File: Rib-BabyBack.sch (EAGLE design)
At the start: 23 parts, among them IC1 REG1117, SW1 DPDT

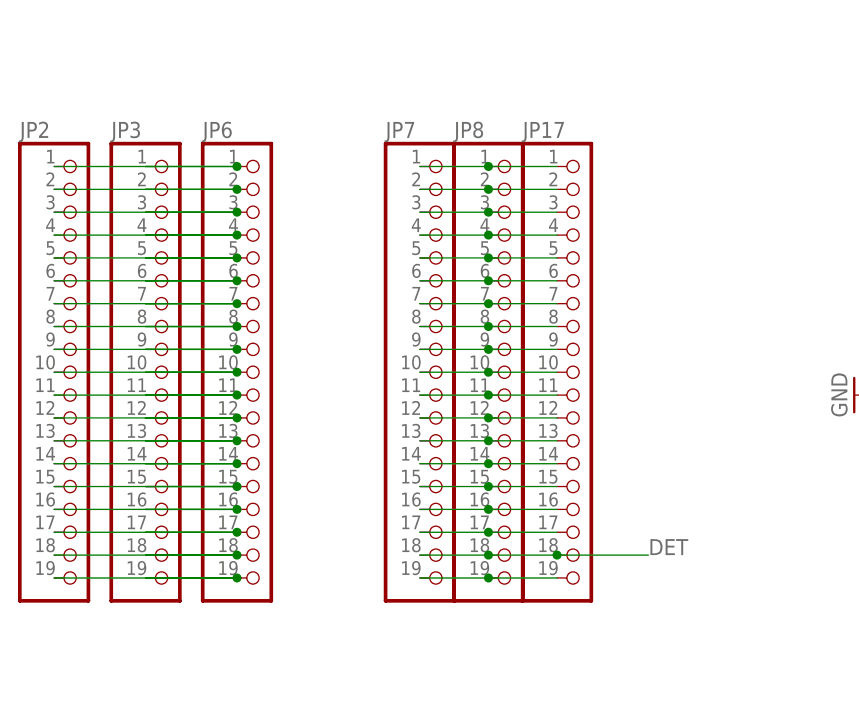
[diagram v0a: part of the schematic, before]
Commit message: Issue #26 Disconnect specific IO used by System Resources on ESP32
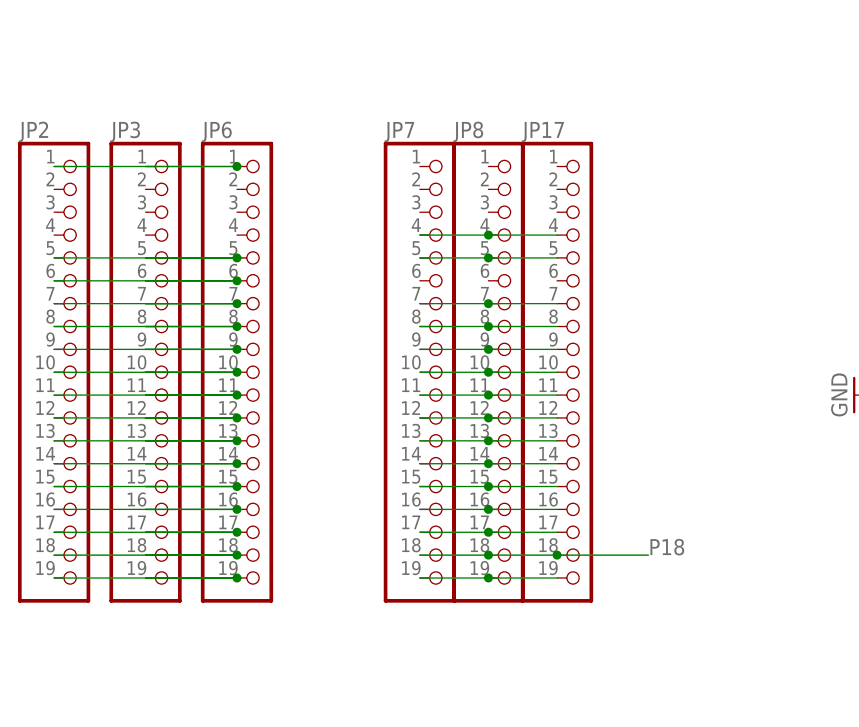
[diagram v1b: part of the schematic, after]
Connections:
- removed net N$14: JP2.9, JP3.9, JP6.9
- removed net N$25: JP17.1, JP7.1, JP8.1
- removed net N$26: JP17.2, JP7.2, JP8.2
- removed net N$27: JP17.3, JP7.3, JP8.3
- removed net N$30: JP17.6, JP7.6, JP8.6
- removed net N$7: JP2.2, JP3.2, JP6.2
- removed net N$8: JP2.3, JP3.3, JP6.3
- removed net N$9: JP2.4, JP3.4, JP6.4
- new net P18: JP17.18, JP7.18, JP8.18
- net DET: now also JP2.9, JP3.9, JP6.9; no longer JP17.18, JP7.18, JP8.18
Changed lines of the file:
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@@
-</segment>
-</net>
-<net name="N$7" class="0">
-<segment>
-<pinref part="JP2" gate="G$1" pin="2"/>
-<pinref part="JP3" gate="G$1" pin="2"/>
-<wire x1="-78.74" y1="-152.4" x2="-58.42" y2="-152.4" width="0.1524" layer="91"/>
-<pinref part="JP6" gate="G$1" pin="2"/>
-<junction x="-58.42" y="-152.4"/>
-<wire x1="-58.42" y1="-152.4" x2="-68.58" y2="-152.4" width="0.1524" layer="91"/>
-</segment>
-</net>
-<net name="N$8" class="0">
-<segment>
-<pinref part="JP2" gate="G$1" pin="3"/>
-<pinref part="JP3" gate="G$1" pin="3"/>
-<wire x1="-78.74" y1="-154.94" x2="-58.42" y2="-154.94" width="0.1524" layer="91"/>
-<pinref part="JP6" gate="G$1" pin="3"/>
-<junction x="-58.42" y="-154.94"/>
-<wire x1="-58.42" y1="-154.94" x2="-68.58" y2="-154.94" width="0.1524" layer="91"/>
-</segment>
-</net>
-<net name="N$9" class="0">
-<segment>
-<pinref part="JP2" gate="G$1" pin="4"/>
-<pinref part="JP3" gate="G$1" pin="4"/>
-<wire x1="-78.74" y1="-157.48" x2="-58.42" y2="-157.48" width="0.1524" layer="91"/>
-<pinref part="JP6" gate="G$1" pin="4"/>
-<junction x="-58.42" y="-157.48"/>
-<wire x1="-58.42" y1="-157.48" x2="-68.58" y2="-157.48" width="0.1524" layer="91"/>
 </segment>
 </net>
@@
 </segment>
 </net>
-<net name="N$14" class="0">
-<segment>
-<pinref part="JP2" gate="G$1" pin="9"/>
-<pinref part="JP3" gate="G$1" pin="9"/>
-<wire x1="-78.74" y1="-170.18" x2="-58.42" y2="-170.18" width="0.1524" layer="91"/>
-<pinref part="JP6" gate="G$1" pin="9"/>
-<junction x="-58.42" y="-170.18"/>
-<wire x1="-58.42" y1="-170.18" x2="-68.58" y2="-170.18" width="0.1524" layer="91"/>
-</segment>
-</net>
 <net name="N$15" class="0">
 <segment>
@@
 </segment>
 </net>
-<net name="N$25" class="0">
-<segment>
-<pinref part="JP8" gate="G$1" pin="1"/>
-<pinref part="JP17" gate="G$1" pin="1"/>
-<wire x1="-22.86" y1="-149.86" x2="-30.48" y2="-149.86" width="0.1524" layer="91"/>
-<pinref part="JP7" gate="G$1" pin="1"/>
-<junction x="-30.48" y="-149.86"/>
-<wire x1="-30.48" y1="-149.86" x2="-38.1" y2="-149.86" width="0.1524" layer="91"/>
-</segment>
-</net>
-<net name="N$26" class="0">
-<segment>
-<pinref part="JP8" gate="G$1" pin="2"/>
-<pinref part="JP17" gate="G$1" pin="2"/>
-<wire x1="-22.86" y1="-152.4" x2="-30.48" y2="-152.4" width="0.1524" layer="91"/>
-<pinref part="JP7" gate="G$1" pin="2"/>
-<junction x="-30.48" y="-152.4"/>
-<wire x1="-30.48" y1="-152.4" x2="-38.1" y2="-152.4" width="0.1524" layer="91"/>
-</segment>
-</net>
-<net name="N$27" class="0">
-<segment>
-<pinref part="JP8" gate="G$1" pin="3"/>
-<pinref part="JP17" gate="G$1" pin="3"/>
-<wire x1="-22.86" y1="-154.94" x2="-30.48" y2="-154.94" width="0.1524" layer="91"/>
-<pinref part="JP7" gate="G$1" pin="3"/>
-<junction x="-30.48" y="-154.94"/>
-<wire x1="-30.48" y1="-154.94" x2="-38.1" y2="-154.94" width="0.1524" layer="91"/>
-</segment>
-</net>
 <net name="N$28" class="0">
 <segment>
@@
 <junction x="-30.48" y="-160.02"/>
 <wire x1="-30.48" y1="-160.02" x2="-38.1" y2="-160.02" width="0.1524" layer="91"/>
-</segment>
-</net>
-<net name="N$30" class="0">
-<segment>
-<pinref part="JP8" gate="G$1" pin="6"/>
-<pinref part="JP17" gate="G$1" pin="6"/>
-<wire x1="-22.86" y1="-162.56" x2="-30.48" y2="-162.56" width="0.1524" layer="91"/>
-<pinref part="JP7" gate="G$1" pin="6"/>
-<junction x="-30.48" y="-162.56"/>
-<wire x1="-30.48" y1="-162.56" x2="-38.1" y2="-162.56" width="0.1524" layer="91"/>
 </segment>
 </net>
@@
 <net name="DET" class="0">
 <segment>
+<pinref part="U$5" gate="G$1" pin="ATT"/>
+<wire x1="30.48" y1="-177.8" x2="20.32" y2="-177.8" width="0.1524" layer="91"/>
+</segment>
+<segment>
+<pinref part="JP2" gate="G$1" pin="9"/>
+<pinref part="JP3" gate="G$1" pin="9"/>
+<wire x1="-78.74" y1="-170.18" x2="-58.42" y2="-170.18" width="0.1524" layer="91"/>
+<pinref part="JP6" gate="G$1" pin="9"/>
+<junction x="-58.42" y="-170.18"/>
+<wire x1="-58.42" y1="-170.18" x2="-68.58" y2="-170.18" width="0.1524" layer="91"/>
+</segment>
+</net>
+<net name="N$24" class="0">
+<segment>
+<pinref part="R1" gate="G$1" pin="1"/>
+<pinref part="LED1" gate="G$1" pin="A"/>
+<wire x1="96.52" y1="-106.68" x2="96.52" y2="-109.22" width="0.1524" layer="91"/>
+</segment>
+</net>
+<net name="N$37" class="0">
+<segment>
+<pinref part="R2" gate="G$1" pin="1"/>
+<pinref part="LED2" gate="G$1" pin="A"/>
+<wire x1="111.76" y1="-106.68" x2="111.76" y2="-109.22" width="0.1524" layer="91"/>
+</segment>
+</net>
+<net name="N$38" class="0">
+<segment>
+<pinref part="R3" gate="G$1" pin="1"/>
+<pinref part="LED3" gate="G$1" pin="A"/>
+<wire x1="127" y1="-106.68" x2="127" y2="-109.22" width="0.1524" layer="91"/>
+</segment>
+</net>
+<net name="P18" class="0">
+<segment>
 <pinref part="JP17" gate="G$1" pin="18"/>
 <pinref part="JP8" gate="G$1" pin="18"/>
@@
 <label x="-12.7" y="-193.04" size="1.778" layer="95"/>
 </segment>
-<segment>
-<pinref part="U$5" gate="G$1" pin="ATT"/>
-<wire x1="30.48" y1="-177.8" x2="20.32" y2="-177.8" width="0.1524" layer="91"/>
-</segment>
-</net>
-<net name="N$24" class="0">
-<segment>
-<pinref part="R1" gate="G$1" pin="1"/>
-<pinref part="LED1" gate="G$1" pin="A"/>
-<wire x1="96.52" y1="-106.68" x2="96.52" y2="-109.22" width="0.1524" layer="91"/>
-</segment>
-</net>
-<net name="N$37" class="0">
-<segment>
-<pinref part="R2" gate="G$1" pin="1"/>
-<pinref part="LED2" gate="G$1" pin="A"/>
-<wire x1="111.76" y1="-106.68" x2="111.76" y2="-109.22" width="0.1524" layer="91"/>
-</segment>
-</net>
-<net name="N$38" class="0">
-<segment>
-<pinref part="R3" gate="G$1" pin="1"/>
-<pinref part="LED3" gate="G$1" pin="A"/>
-<wire x1="127" y1="-106.68" x2="127" y2="-109.22" width="0.1524" layer="91"/>
-</segment>
-</net>
+</net>

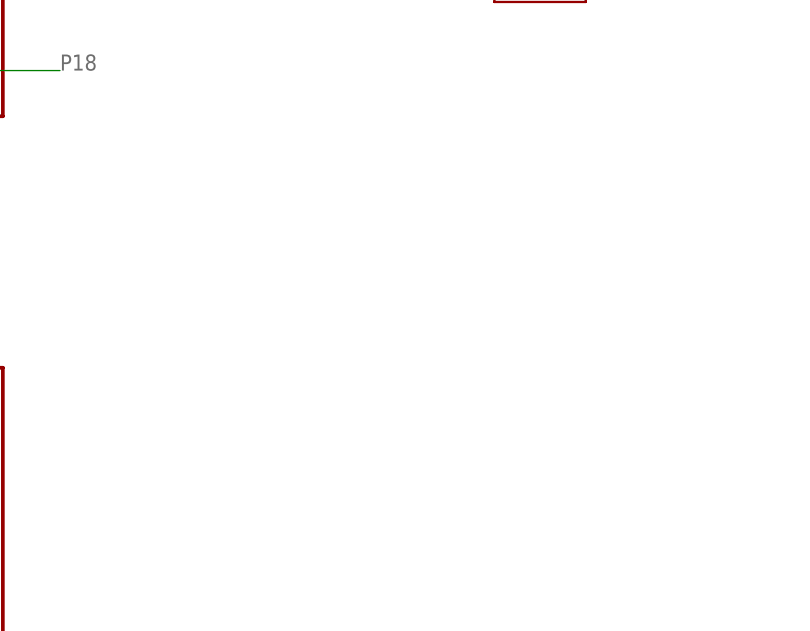
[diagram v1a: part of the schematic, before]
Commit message: Issue #32 ESP32 needs a user accessible LED on 13
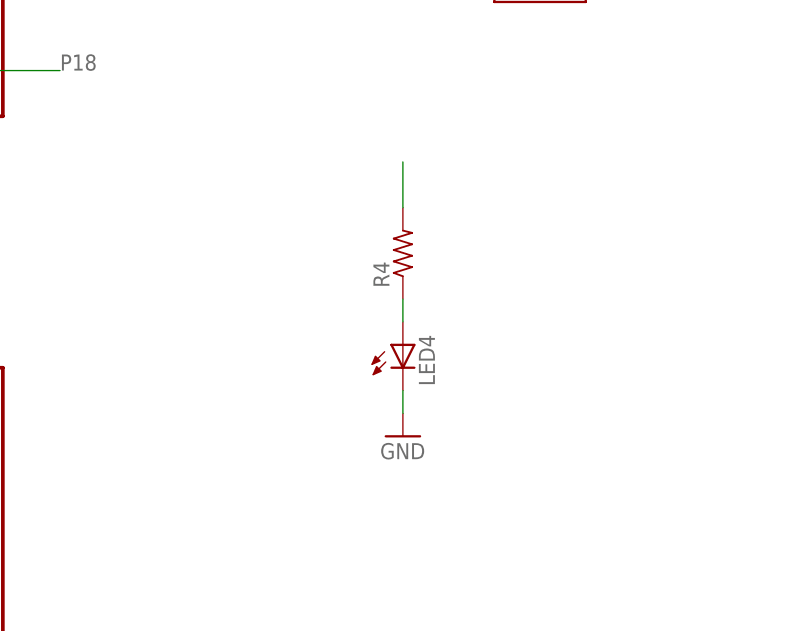
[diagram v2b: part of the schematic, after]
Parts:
- added LED4: (no value), eagle-ltspice:LED_ESML0603
- added R4: (no value), resistor:R-US_R0603
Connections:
- removed net N$10: JP2.5, JP3.5, JP6.5
- new net N$1: LED4.A, R4.1
- new net P13: JP2.5, JP3.5, JP6.5, R4.2
- net GND: now also LED4.C
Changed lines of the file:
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@@
 <part name="R2" library="resistor" library_urn="urn:adsk.eagle:library:348" deviceset="R-US_" device="R0603" package3d_urn="urn:adsk.eagle:package:26057/1"/>
 <part name="R3" library="resistor" library_urn="urn:adsk.eagle:library:348" deviceset="R-US_" device="R0603" package3d_urn="urn:adsk.eagle:package:26057/1"/>
+<part name="LED4" library="eagle-ltspice" library_urn="urn:adsk.eagle:library:217" deviceset="LED_E" device="SML0603" package3d_urn="urn:adsk.eagle:package:13315/1"/>
+<part name="GND6" library="supply1" library_urn="urn:adsk.eagle:library:371" deviceset="GND" device=""/>
+<part name="R4" library="resistor" library_urn="urn:adsk.eagle:library:348" deviceset="R-US_" device="R0603" package3d_urn="urn:adsk.eagle:package:26057/1"/>
 </parts>
 <sheets>
@@
 <instance part="R2" gate="G$1" x="111.76" y="-101.6" rot="R90"/>
 <instance part="R3" gate="G$1" x="127" y="-101.6" rot="R90"/>
+<instance part="LED4" gate="G$1" x="25.4" y="-223.52"/>
+<instance part="GND6" gate="1" x="25.4" y="-233.68"/>
+<instance part="R4" gate="G$1" x="25.4" y="-213.36" rot="R90"/>
 </instances>
 <busses>
@@
 <segment>
 <wire x1="55.88" y1="33.02" x2="50.8" y2="33.02" width="0.1524" layer="91"/>
-</segment>
-</net>
-<net name="N$10" class="0">
-<segment>
-<pinref part="JP2" gate="G$1" pin="5"/>
-<pinref part="JP3" gate="G$1" pin="5"/>
-<wire x1="-78.74" y1="-160.02" x2="-58.42" y2="-160.02" width="0.1524" layer="91"/>
-<pinref part="JP6" gate="G$1" pin="5"/>
-<junction x="-58.42" y="-160.02"/>
-<wire x1="-58.42" y1="-160.02" x2="-68.58" y2="-160.02" width="0.1524" layer="91"/>
 </segment>
 </net>
@@
 <wire x1="96.52" y1="-116.84" x2="96.52" y2="-119.38" width="0.1524" layer="91"/>
 </segment>
+<segment>
+<pinref part="LED4" gate="G$1" pin="C"/>
+<pinref part="GND6" gate="1" pin="GND"/>
+<wire x1="25.4" y1="-228.6" x2="25.4" y2="-231.14" width="0.1524" layer="91"/>
+</segment>
 </net>
 <net name="VCC" class="0">
@@
 </segment>
 </net>
+<net name="P13" class="0">
+<segment>
+<pinref part="R4" gate="G$1" pin="2"/>
+<wire x1="25.4" y1="-208.28" x2="25.4" y2="-203.2" width="0.1524" layer="91"/>
+</segment>
+<segment>
+<pinref part="JP2" gate="G$1" pin="5"/>
+<pinref part="JP3" gate="G$1" pin="5"/>
+<wire x1="-78.74" y1="-160.02" x2="-58.42" y2="-160.02" width="0.1524" layer="91"/>
+<pinref part="JP6" gate="G$1" pin="5"/>
+<junction x="-58.42" y="-160.02"/>
+<wire x1="-58.42" y1="-160.02" x2="-68.58" y2="-160.02" width="0.1524" layer="91"/>
+</segment>
+</net>
+<net name="N$1" class="0">
+<segment>
+<pinref part="R4" gate="G$1" pin="1"/>
+<pinref part="LED4" gate="G$1" pin="A"/>
+<wire x1="25.4" y1="-218.44" x2="25.4" y2="-220.98" width="0.1524" layer="91"/>
+</segment>
+</net>

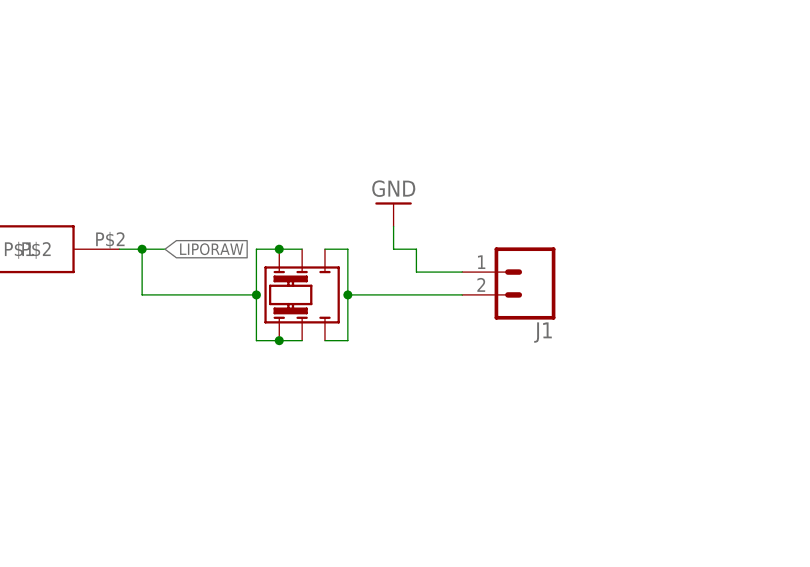
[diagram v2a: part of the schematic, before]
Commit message: Issue #22 Solder lugs resized to 3MM diameter holes and moved
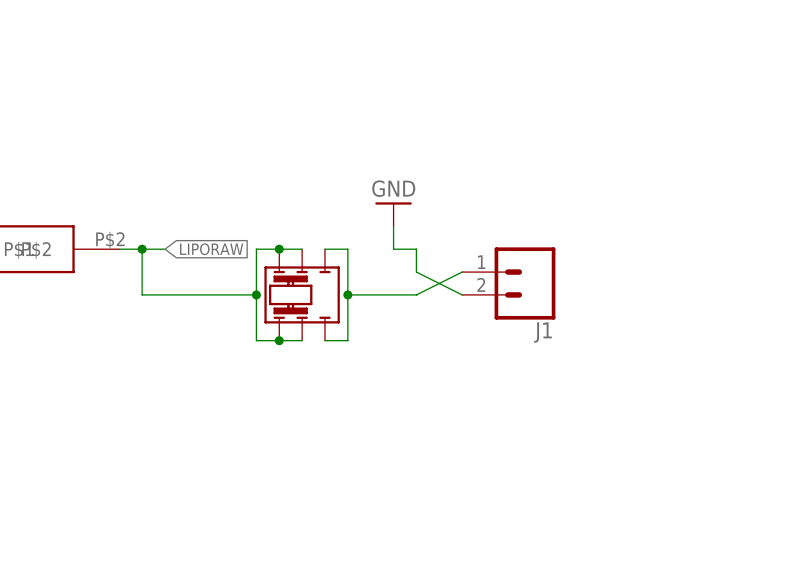
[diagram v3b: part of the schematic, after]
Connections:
- net GND: now also J1.2; no longer J1.1
- net N$11: now also J1.1; no longer J1.2
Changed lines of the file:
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@@
 <wire x1="71.12" y1="-53.34" x2="71.12" y2="-55.88" width="0.1524" layer="91"/>
 <wire x1="71.12" y1="-55.88" x2="73.66" y2="-55.88" width="0.1524" layer="91"/>
-<pinref part="J1" gate="G$1" pin="1"/>
-<wire x1="78.74" y1="-58.42" x2="73.66" y2="-58.42" width="0.1524" layer="91"/>
 <wire x1="73.66" y1="-58.42" x2="73.66" y2="-55.88" width="0.1524" layer="91"/>
+<pinref part="J1" gate="G$1" pin="2"/>
+<wire x1="78.74" y1="-60.96" x2="73.66" y2="-58.42" width="0.1524" layer="91"/>
 </segment>
 <segment>
@@
 <segment>
 <wire x1="66.04" y1="-66.04" x2="66.04" y2="-60.96" width="0.1524" layer="91"/>
+<pinref part="SW1" gate="G$1" pin="C2"/>
 <wire x1="66.04" y1="-60.96" x2="66.04" y2="-55.88" width="0.1524" layer="91"/>
-<wire x1="78.74" y1="-60.96" x2="66.04" y2="-60.96" width="0.1524" layer="91"/>
-<junction x="66.04" y="-60.96"/>
-<pinref part="SW1" gate="G$1" pin="C2"/>
 <wire x1="66.04" y1="-66.04" x2="63.5" y2="-66.04" width="0.1524" layer="91"/>
 <pinref part="SW1" gate="G$1" pin="C1"/>
 <wire x1="66.04" y1="-55.88" x2="63.5" y2="-55.88" width="0.1524" layer="91"/>
-<pinref part="J1" gate="G$1" pin="2"/>
-</segment>
-</net>
+<wire x1="66.04" y1="-60.96" x2="73.66" y2="-60.96" width="0.1524" layer="91"/>
+<junction x="66.04" y="-60.96"/>
+<pinref part="J1" gate="G$1" pin="1"/>
+<wire x1="73.66" y1="-60.96" x2="78.74" y2="-58.42" width="0.1524" layer="91"/>
+</segment>
+</net>

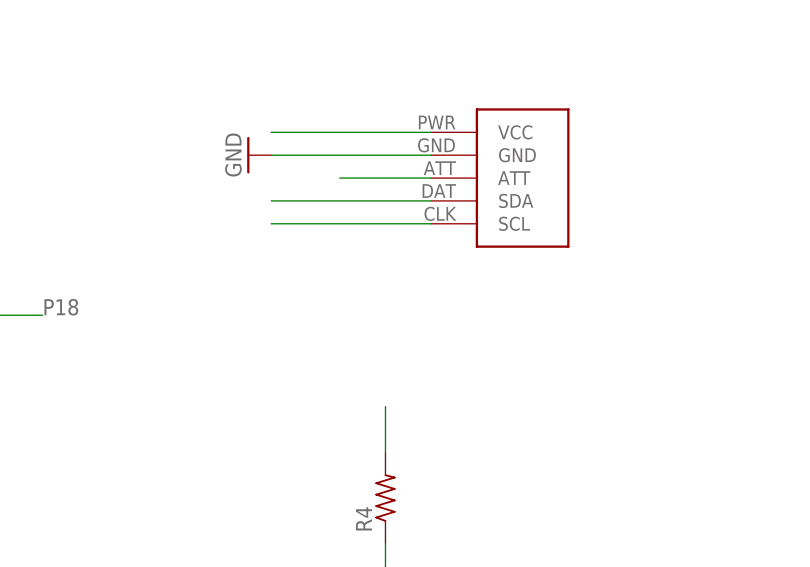
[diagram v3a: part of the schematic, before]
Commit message: Issue #19 4k7 ohm pullups to 3.3v are needed on SDA and SCL
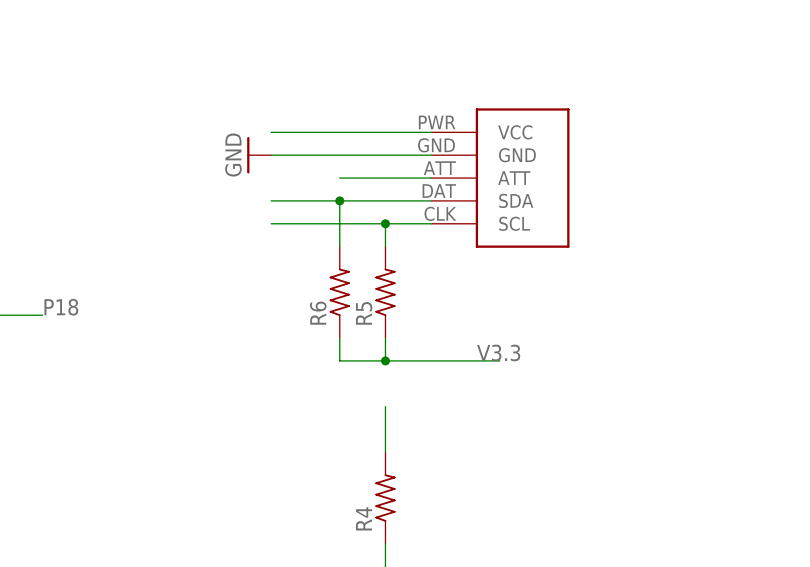
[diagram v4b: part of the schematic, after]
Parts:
- added R5, R6: (no value), resistor:R-US_R0603
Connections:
- net SCL: now also R5.2
- net SDA: now also R6.2
- net V3.3: now also R5.1, R6.1
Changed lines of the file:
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@@
 <part name="GND6" library="supply1" library_urn="urn:adsk.eagle:library:371" deviceset="GND" device=""/>
 <part name="R4" library="resistor" library_urn="urn:adsk.eagle:library:348" deviceset="R-US_" device="R0603" package3d_urn="urn:adsk.eagle:package:26057/1"/>
+<part name="R5" library="resistor" library_urn="urn:adsk.eagle:library:348" deviceset="R-US_" device="R0603" package3d_urn="urn:adsk.eagle:package:26057/1"/>
+<part name="R6" library="resistor" library_urn="urn:adsk.eagle:library:348" deviceset="R-US_" device="R0603" package3d_urn="urn:adsk.eagle:package:26057/1"/>
 </parts>
 <sheets>
@@
 <instance part="GND6" gate="1" x="25.4" y="-233.68"/>
 <instance part="R4" gate="G$1" x="25.4" y="-213.36" rot="R90"/>
+<instance part="R5" gate="G$1" x="25.4" y="-190.5" rot="R90"/>
+<instance part="R6" gate="G$1" x="20.32" y="-190.5" rot="R90"/>
 </instances>
 <busses>
@@
 <segment>
 <pinref part="U$5" gate="G$1" pin="SDA"/>
-<wire x1="30.48" y1="-180.34" x2="12.7" y2="-180.34" width="0.1524" layer="91"/>
+<wire x1="30.48" y1="-180.34" x2="20.32" y2="-180.34" width="0.1524" layer="91"/>
+<pinref part="R6" gate="G$1" pin="2"/>
+<wire x1="20.32" y1="-180.34" x2="12.7" y2="-180.34" width="0.1524" layer="91"/>
+<wire x1="20.32" y1="-185.42" x2="20.32" y2="-180.34" width="0.1524" layer="91"/>
+<junction x="20.32" y="-180.34"/>
 </segment>
 <segment>
@@
 <segment>
 <pinref part="U$5" gate="G$1" pin="SCL"/>
-<wire x1="30.48" y1="-182.88" x2="12.7" y2="-182.88" width="0.1524" layer="91"/>
+<wire x1="30.48" y1="-182.88" x2="25.4" y2="-182.88" width="0.1524" layer="91"/>
+<pinref part="R5" gate="G$1" pin="2"/>
+<wire x1="25.4" y1="-182.88" x2="12.7" y2="-182.88" width="0.1524" layer="91"/>
+<wire x1="25.4" y1="-185.42" x2="25.4" y2="-182.88" width="0.1524" layer="91"/>
+<junction x="25.4" y="-182.88"/>
 </segment>
 <segment>
@@
 <wire x1="127" y1="-96.52" x2="127" y2="-91.44" width="0.1524" layer="91"/>
 </segment>
-</net>
+<segment>
+<pinref part="R6" gate="G$1" pin="1"/>
+<wire x1="20.32" y1="-195.58" x2="20.32" y2="-198.12" width="0.1524" layer="91"/>
+<wire x1="20.32" y1="-198.12" x2="25.4" y2="-198.12" width="0.1524" layer="91"/>
+<pinref part="R5" gate="G$1" pin="1"/>
+<wire x1="25.4" y1="-198.12" x2="38.1" y2="-198.12" width="0.1524" layer="91"/>
+<wire x1="25.4" y1="-195.58" x2="25.4" y2="-198.12" width="0.1524" layer="91"/>
+<junction x="25.4" y="-198.12"/>
+<label x="35.56" y="-198.12" size="1.778" layer="95"/>
+</segment>
+</net>
